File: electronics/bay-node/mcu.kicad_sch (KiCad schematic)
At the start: 15 parts, among them SW1 RESET, SW2 BOOT, U3 ESP32-S3-MINI-1-N8

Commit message: BOM: bulk hardware prices, JLC PCBA type per board
- hardware at bulk prices (T-nuts, screws, heat-set inserts, corner
  brackets), generic USB-C panel extensions; drop the label tape (the
  printed bay_label fills the drawer recess); heat-set inserts for camera
  pods only where a camera hangs
- catalog: standard_only flag (ESP32-S3-MINI-1, WS2812B-2020 cannot be
  placed with JLC Economic PCBA); bom.py prices Standard PCBA for the
  bay node and Economic for the power hub
- electrolytics moved to the Economic-capable LCSC listings of the same
  parts (C3352, C3358); PCB footprint fields synced, ERC/DRC/parity clean
- docs: JLC assembly notes (no Basic drop-ins for the extended parts)

Total ~EUR 927 -> ~EUR 828 (EUR 66 -> 59 per bay).

Co-Authored-By: Claude Opus 5.5 <noreply@anthropic.com>
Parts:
- D4: Alternative (none) -> WS2812C-2020-V6 (C55109522) is Economic-PCBA capable; check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
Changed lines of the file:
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@@
+			)
+		)
+		(property "Alternative" "WS2812C-2020-V6 (C55109522) is Economic-PCBA capable; check its pinout before swapping"
+			(at 45.72 191.77 0)
+			(effects
+				(font
+					(size 1.27 1.27)
+				)
+				(hide yes)
 			)
 		)

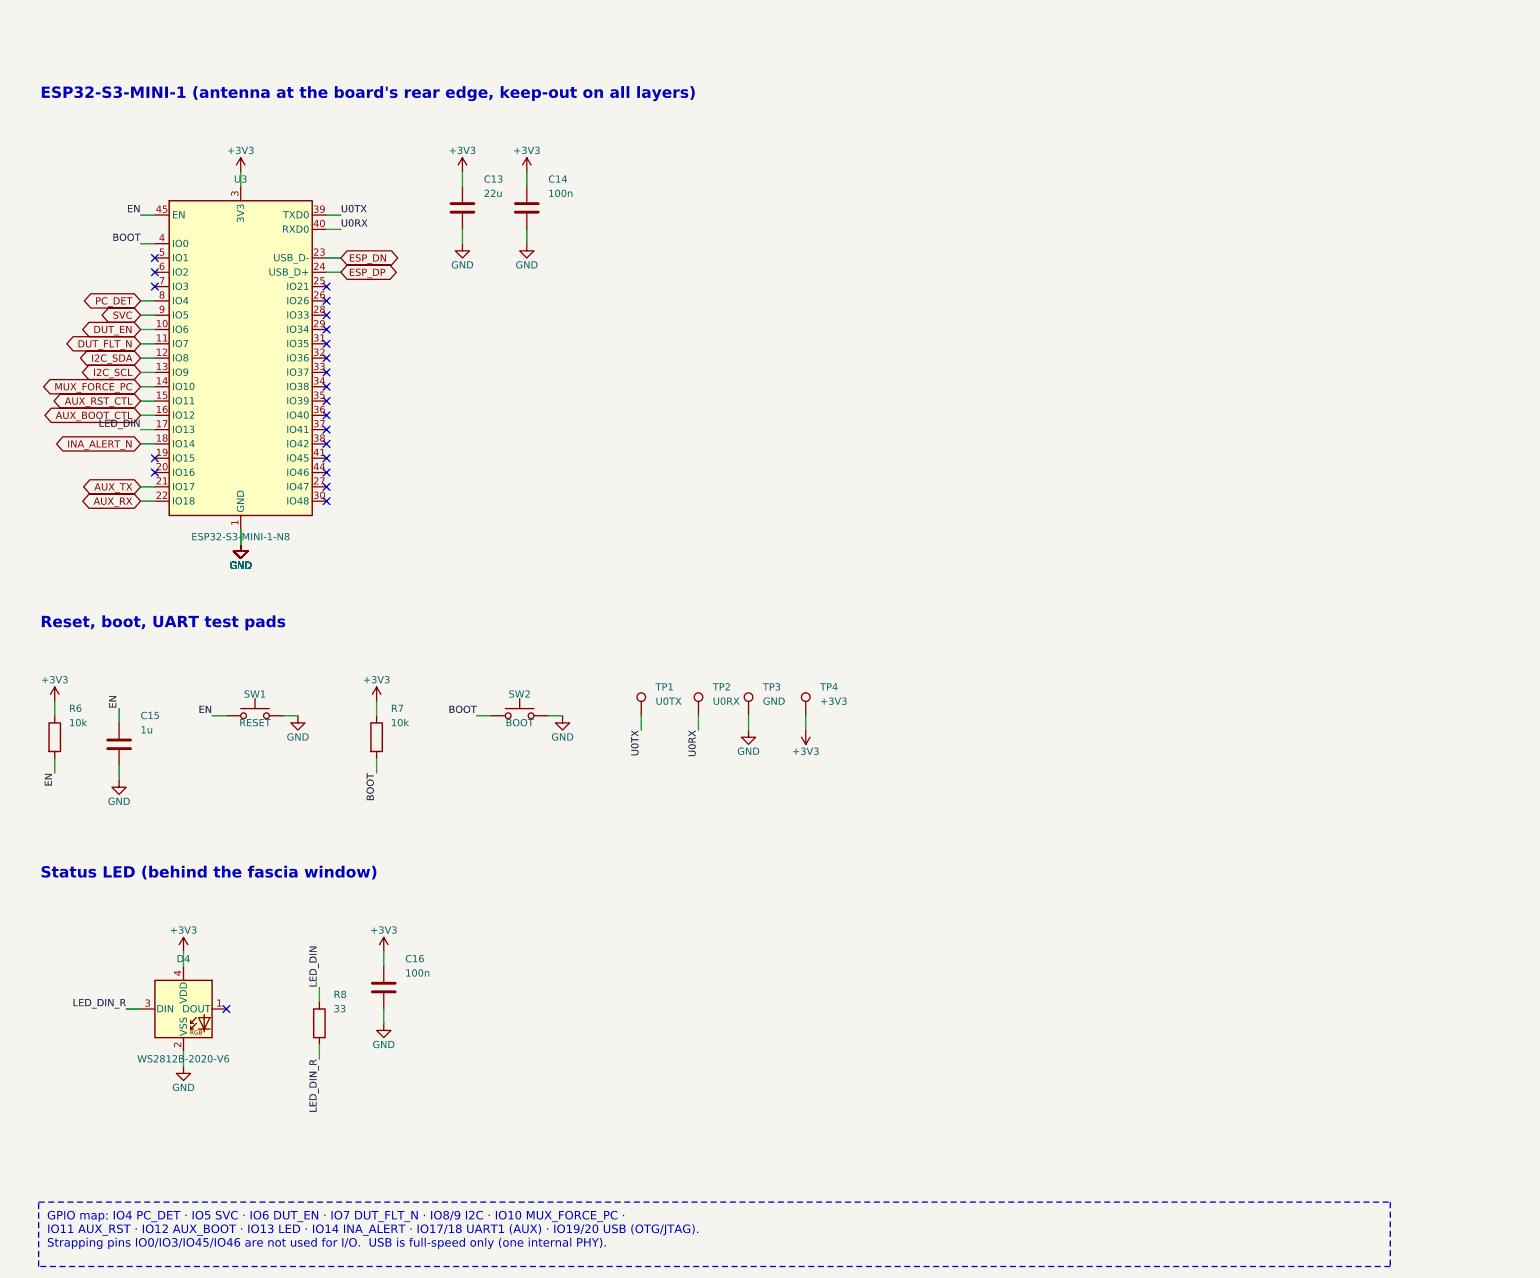
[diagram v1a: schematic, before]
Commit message: Schematics: draw real wires and an overview block diagram
The generator used to connect every pin through a net label only. Now,
in each block, the part with the most pins is the anchor and the
two-pin parts that share a signal with one of its side pins hang off
that pin on a real wire; parts chained behind them (R -> C -> GND)
stack underneath, and anchor-less blocks (pull-ups, reset/boot
buttons) are adopted by the anchor they connect to. Power symbols on
side pins point outward; power-flag references are hidden.

The root sheet becomes a block diagram: the supply rails each sheet
uses across the top, and one lane per pair of sheets listing the
signals they share.

Every wired net still carries one label, so net names, ERC (0) and the
PCB's schematic parity (0) are unchanged; the routed PCBs are untouched.

Co-Authored-By: Claude Opus 5.5 <noreply@anthropic.com>
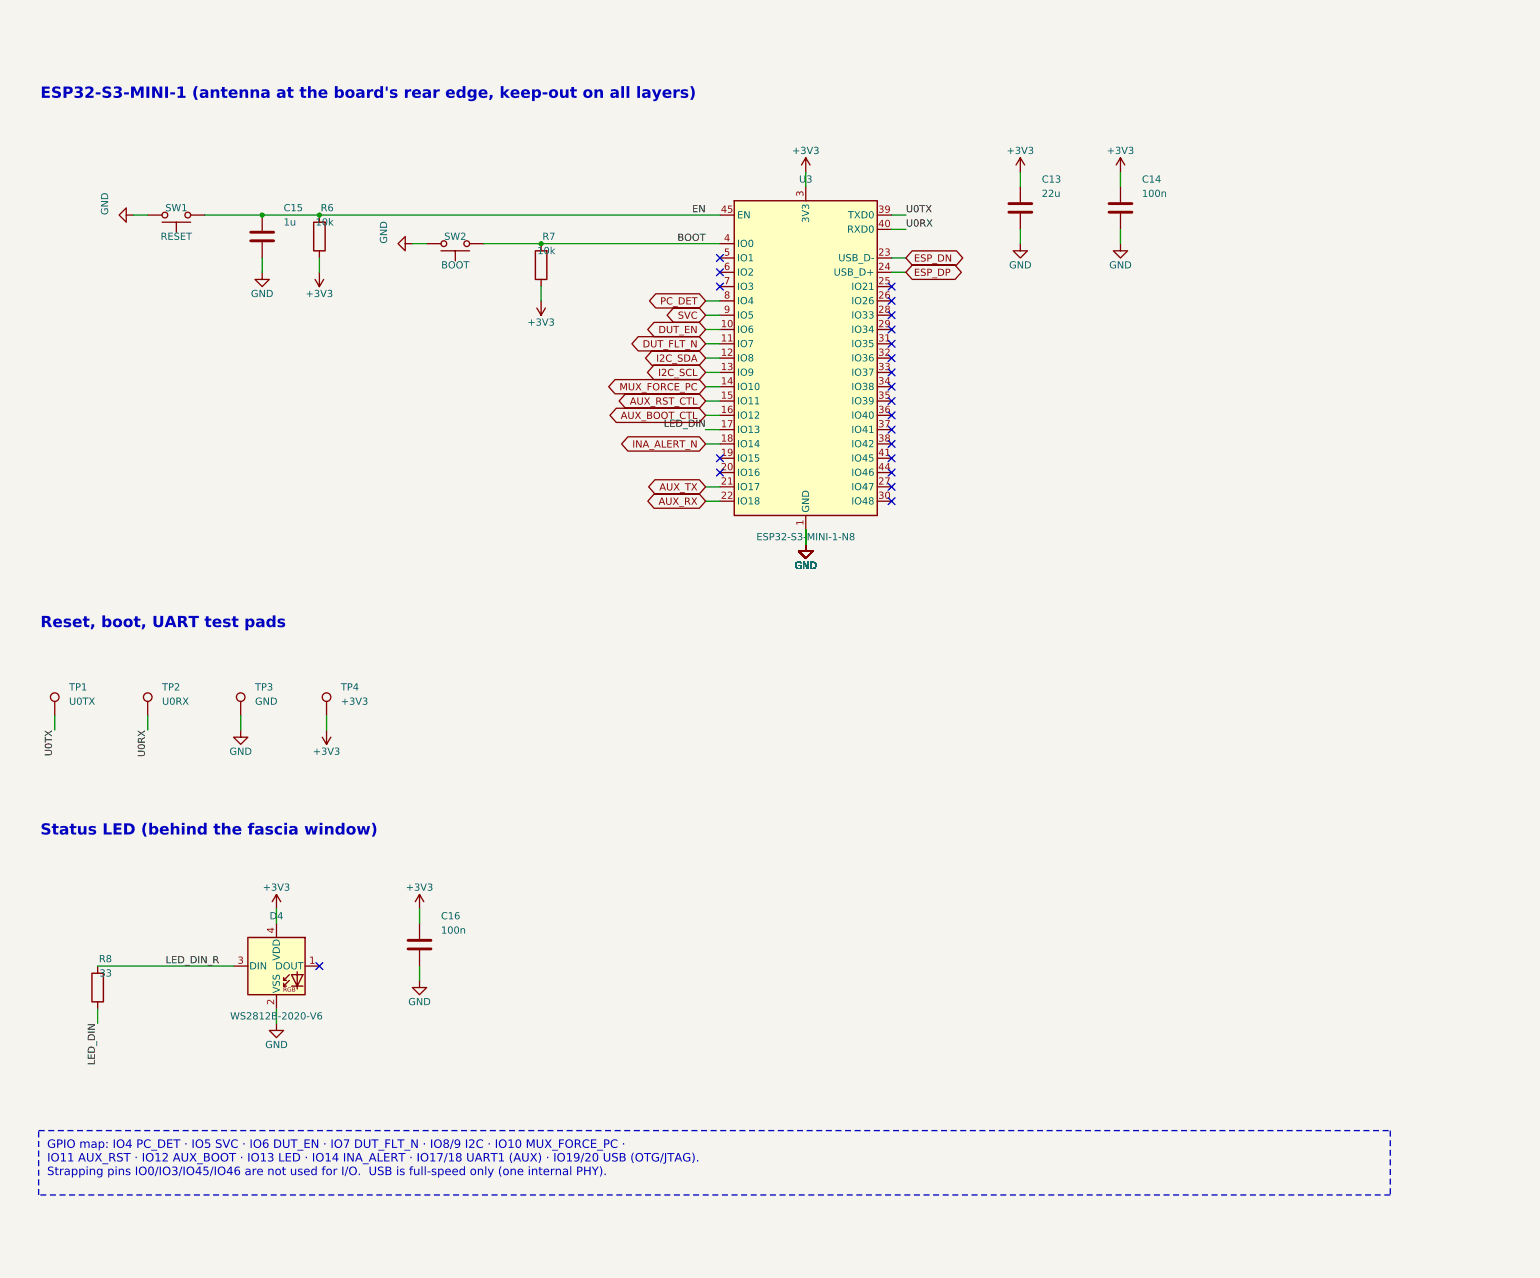
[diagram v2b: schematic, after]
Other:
- moved on the sheet: C13, C14, C15, C16, D4, R6, R7, R8, SW1, SW2, TP1, TP2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

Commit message: Boards v0.2: LMR51635 buck, JST PH, drawn schematics, thermal reliefs
Addresses Fabio's review of v0.1.

Bay node (rev 0.2):
- 5 V buck: LMR51635YDDCR (60 V, 3.5 A, synchronous, 1.1 MHz) with a
  3.3 uH FXL0630, 3 x 22 uF out, 2 x 10 uF + 100 nF in, FB 120k/22k
  (5.16 V), EN 1M/100k UVLO (13.5 V on, 10.8 V off). Replaces the
  TPS54360B, its Schottky and compensation network. CIN straddles the
  VIN/GND pins on solid top-side islands with vias to In1 (TI SLUSF64B).
- 24 V in/out on JST PH (carrier notches resized, rack.yaml pwr_y).
- Power nets named along the path: 24V_BUS -> +24V -> +5V -> DUT_5V_SW
  -> shunt -> DUT_5V; the INA226 visibly runs from +3V3.
- Stackup S+GND / GND / PWR / S+GND: In2 carries +5V, +3V3 under the
  ESP32 and a protected 24 V bus strip. Outer GND pours kept (without
  them Freerouting left ~25 connections unrouted).

Power hub (rev 0.2): JST VH input instead of the screw terminal, JST PH
row outputs, eFuse limit 1.6 A (RILIM 7.5k) to protect the 2 A contacts.

Generator:
- eda.py: drawn schematic mode (sch= placement, Sheet.wire/tag/frame,
  rotated/mirrored symbols, automatic junctions, per-island labels and
  checks that no wire touches another net); all seven sheets redrawn.
- pcbgen.py: thermal reliefs on every pour (+ <board>.kicad_dru for
  single spokes on fine pitch), configurable inner layers, per-zone
  deferral, fixed vias, DRC-driven fix-up for isolated GND pads.
- JLC CPL fix for the LMR51635 (270 deg); BOM, cables, viewer, docs.

ERC 0, DRC 0 copper errors, 0 unconnected, schematic parity 0 on both.

Co-Authored-By: Claude Opus 5.5 <noreply@anthropic.com>
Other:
- note added: "ESP32-S3-MINI-1 (PCB antenna at the board's rear edge: no copper under it, any layer)"
- note added: "Reset and boot"
- note added: "UART test pads"
- note removed: "ESP32-S3-MINI-1 (antenna at the board's rear edge, keep-out on all layers)"
- note removed: "Reset, boot, UART test pads"
- moved on the sheet: C13, C14, C15, C16, D4, R6, R7, R8, SW1, SW2, TP1, TP2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

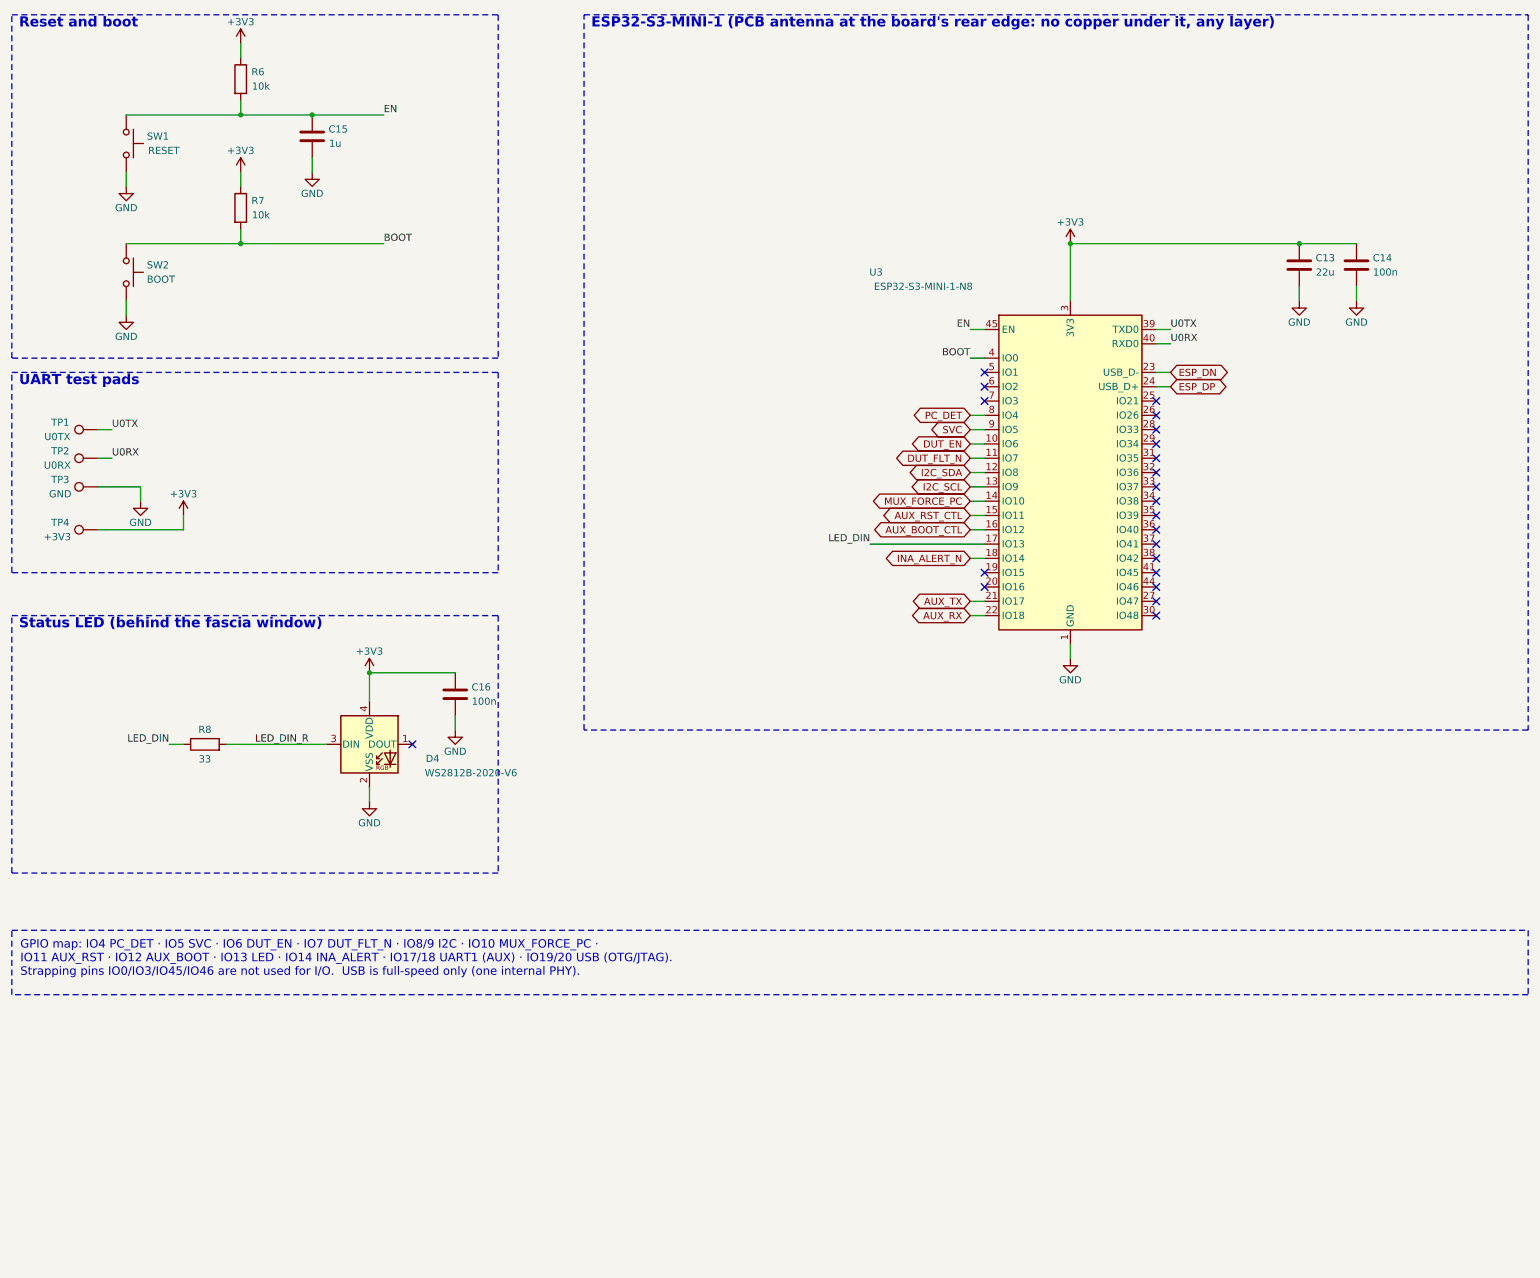
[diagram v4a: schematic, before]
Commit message: Bay node v0.4: In2 power only, re-placed, SMD JST PH, new GPIO map
Fabio's second round: signals / GND / power / signals.  With no signal
on In2, v0.3's placement left 13-18 connections unrouted, mostly GPIOs
leaving the module's left column for the right half.  Connectors and
module stay put; the DUT power block moves to the top right, LDO and
buttons to the top left, the muxes under the module, and each GPIO sits
on the module edge facing its destination (firmware devicetree, README
pin table and docs follow; check_pinmap.py passes).

pcbgen: fanout_nets gives every GND/supply pin its own locked via to
its plane before routing.  USB HS pairs redrawn for the new geometry
(J3 -> J4 skew 0.1 mm).  J1/J2/J5/J6 are now S*B-PH-SM4-TB, placed by
JLC (24 V and GND on solid islands with 4 vias each); UART test pads on
the bottom side.  J5 is a JST PH 6 (Fabio: SH too small).

ERC 0, DRC 0 errors / 0 warnings / 0 unconnected, parity 0 (Konnect).

Co-Authored-By: Claude Opus 5.5 <noreply@anthropic.com>
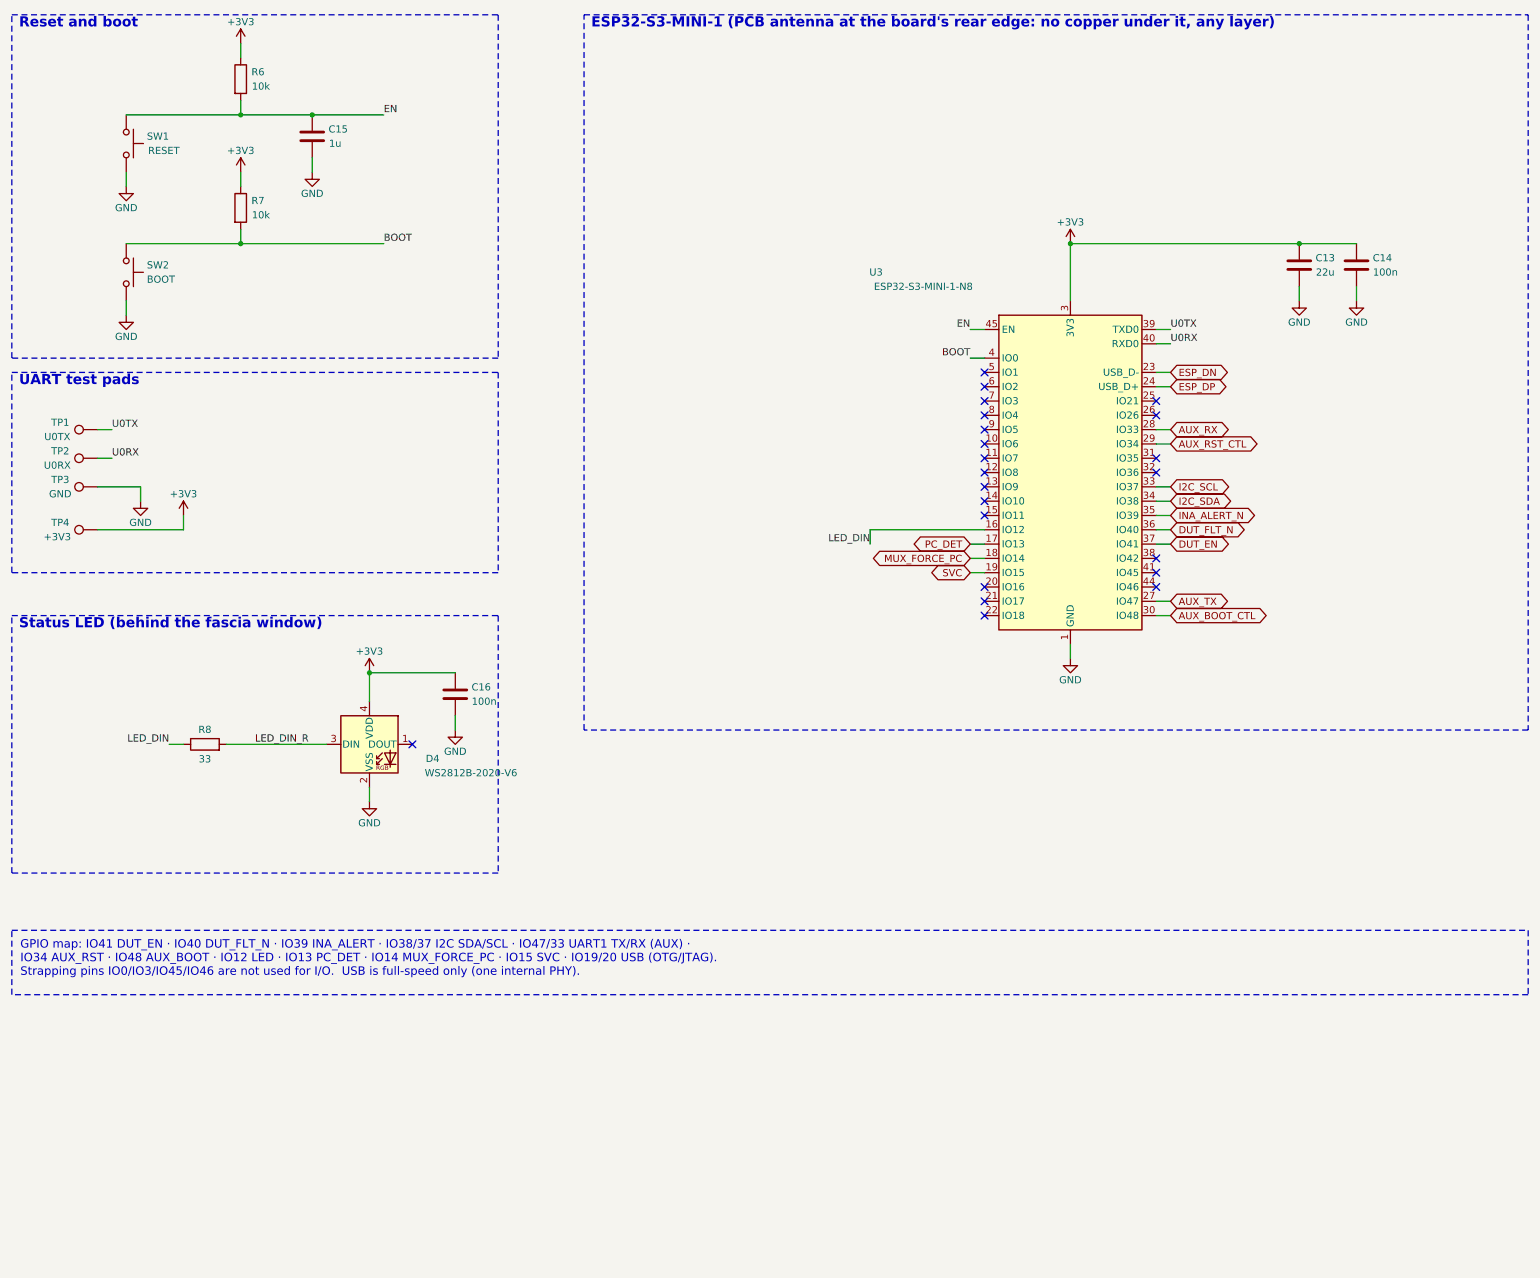
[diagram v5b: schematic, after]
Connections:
- net AUX_BOOT_CTL: now also U3.30 (IO48); no longer U3.16 (IO12)
- net AUX_RST_CTL: now also U3.29 (IO34); no longer U3.15 (IO11)
- net AUX_RX: now also U3.28 (IO33); no longer U3.22 (IO18)
- net AUX_TX: now also U3.27 (IO47); no longer U3.21 (IO17)
- net DUT_EN: now also U3.37 (IO41); no longer U3.10 (IO6)
- net DUT_FLT_N: now also U3.36 (IO40); no longer U3.11 (IO7)
- net I2C_SCL: now also U3.33 (IO37); no longer U3.13 (IO9)
- net I2C_SDA: now also U3.34 (IO38); no longer U3.12 (IO8)
- net INA_ALERT_N: now also U3.35 (IO39); no longer U3.18 (IO14)
- net LED_DIN: now also U3.16 (IO12); no longer U3.17 (IO13)
- net MUX_FORCE_PC: now also U3.18 (IO14); no longer U3.14 (IO10)
- net PC_DET: now also U3.17 (IO13); no longer U3.8 (IO4)
- net SVC: now also U3.19 (IO15); no longer U3.9 (IO5)
